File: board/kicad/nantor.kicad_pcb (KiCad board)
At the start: 2 copper layers, 139.5 x 94.4 mm, 26 parts, among them J1 Bridge, J2 Batt, SW1 Power, SW2 Power, U1 YAAJ_WeAct_BlackPill_Part_Like

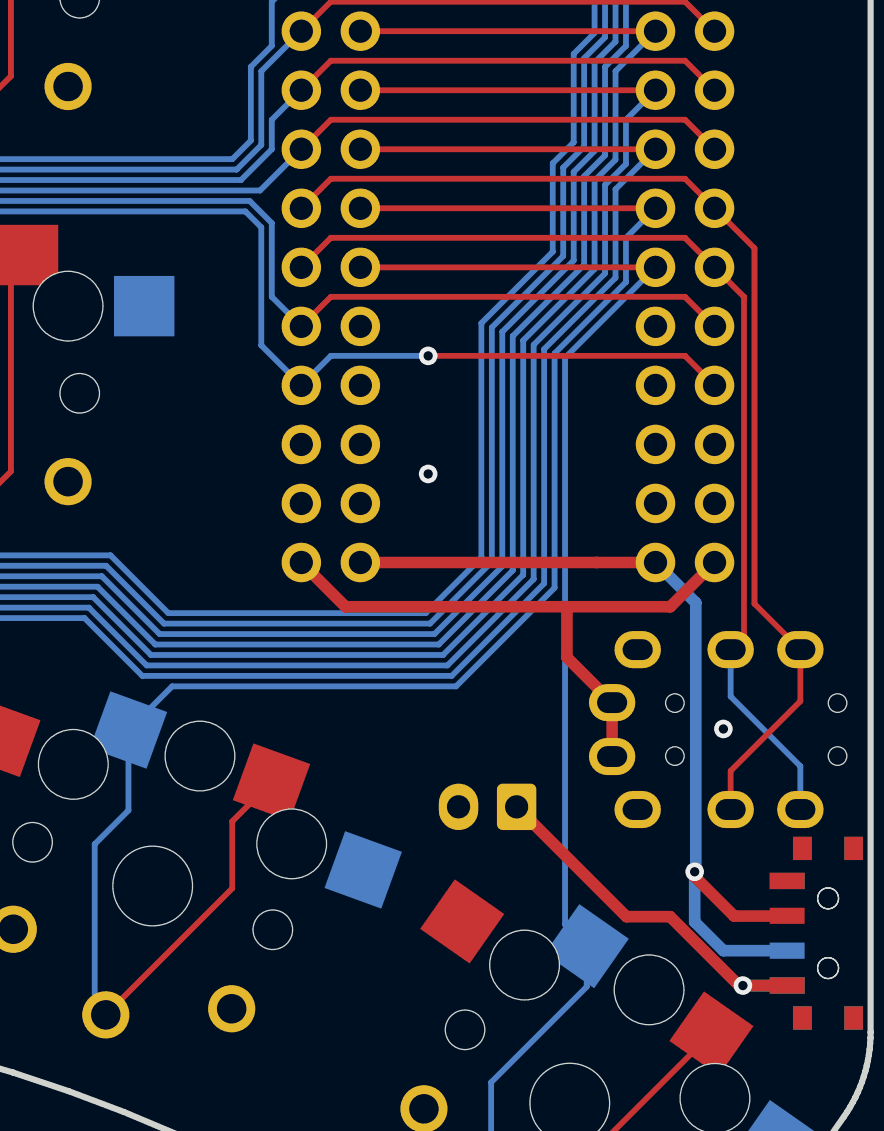
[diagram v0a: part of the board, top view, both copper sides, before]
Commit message: Move battery connector
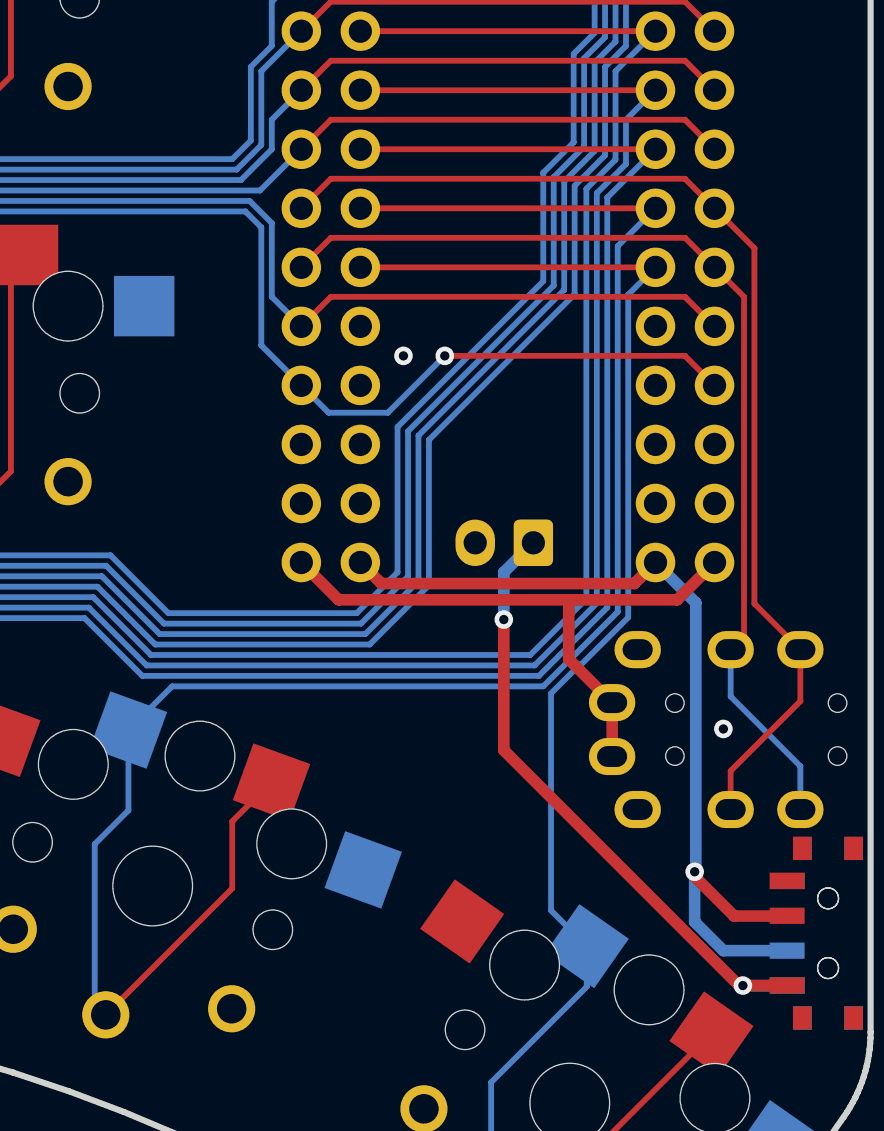
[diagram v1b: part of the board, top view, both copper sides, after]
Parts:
- moved J2 11.4 mm to (193.5, 104.7)
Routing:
- net Net-(J2-Pin_1): track 16.7 -> 27.7 mm, vias 1 -> 2
- net /k35: track 77.7 -> 79.9 mm
- net /k34: track 102.7 -> 104.9 mm
- net /k33: track 127.1 -> 129.3 mm
- net /k21: track 167.5 -> 169.7 mm
- net /k25: track 100.0 -> 98.3 mm
- net /k23: track 135.6 -> 133.8 mm
- net /k24: track 117.3 -> 115.6 mm
- net /k22: track 149.7 -> 148.0 mm
- net /k10: track 169.6 -> 170.5 mm
- net Net-(SW1-B): track 38.3 -> 39.0 mm
- net /k36: track 69.9 -> 70.5 mm

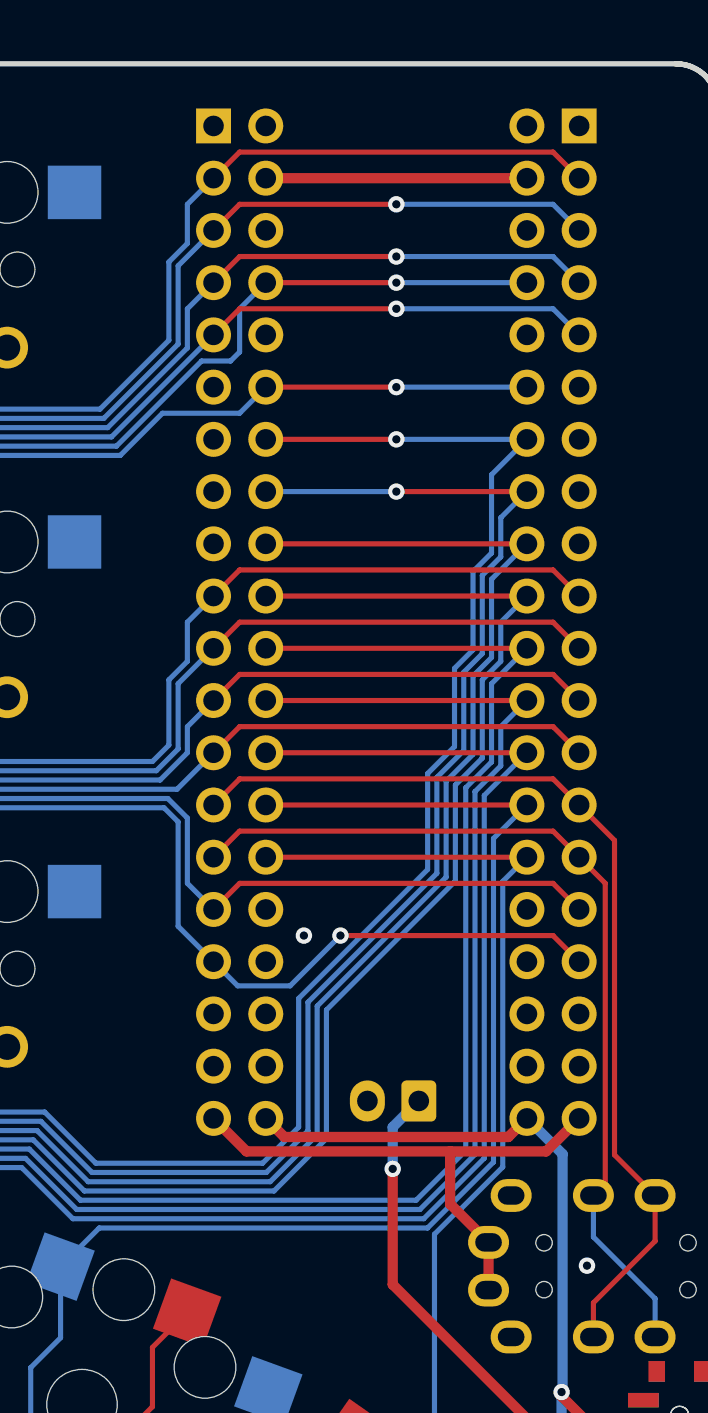
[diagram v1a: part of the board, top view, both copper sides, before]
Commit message: Add LEDs
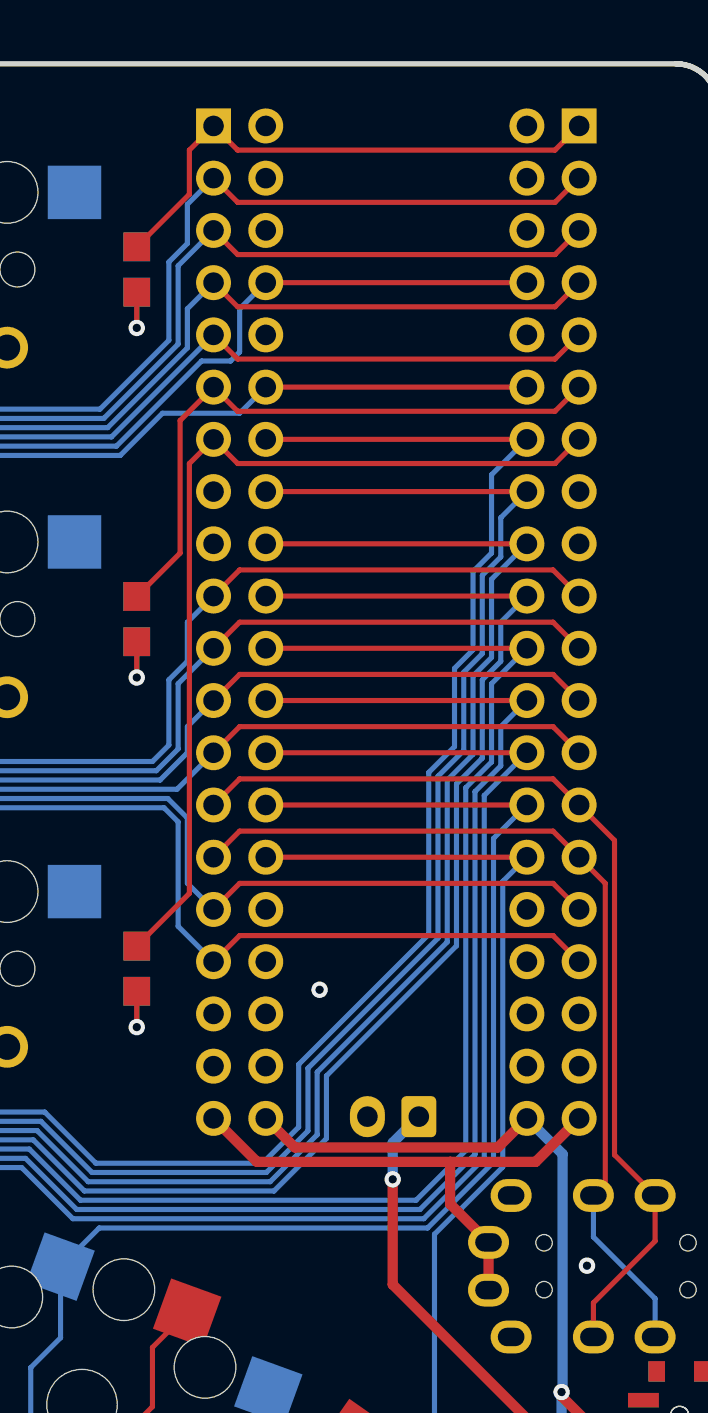
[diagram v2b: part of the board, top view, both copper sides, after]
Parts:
- added D1: LED, nantor:LED_0805, F.Cu at (179.8, 98.3)
- added D2: LED, nantor:LED_0805, F.Cu at (179.8, 81.3)
- added D3: LED, nantor:LED_0805, F.Cu at (179.8, 64.3)
- added R1: R, nantor:LED_0805, B.Cu at (179.8, 98.3)
- added R2: R, nantor:LED_0805, B.Cu at (179.8, 81.3)
- added R3: R, nantor:LED_0805, B.Cu at (179.8, 64.3)
- moved J2 0.76 mm to (193.5, 105.5)
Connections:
- net Net-(J2-Pin_1) renamed /BatPwr
- net Net-(SW1-B) renamed /BatActive
- net Net-(U1-PB6) renamed /TX
- net Net-(U1-PB7) renamed /RX
- U1 pad 1: unconnected-(U1-PB12-Pad1) -> /L3
- U1 pad 6: unconnected-(U1-PA9-Pad6) -> /L2
- U1 pad 7: unconnected-(U1-PA10-Pad7) -> /L1
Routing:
- net /L1: track 0.00 -> 44.9 mm
- net /L2: track 0.00 -> 30.5 mm
- net /L3: track 0.00 -> 26.2 mm
- net GND: track 12.7 -> 0.00 mm
- net Net-(D3-K): track 0.00 -> 3.48 mm, vias 0 -> 1
- net Net-(D2-K): track 0.00 -> 3.48 mm, vias 0 -> 1
- net Net-(D1-K): track 0.00 -> 3.48 mm, vias 0 -> 1
- net /k10: track 170.5 -> 169.6 mm, vias 1 -> 0
- net /BatPwr: track 27.7 -> 27.0 mm
- net /k25: track 98.3 -> 98.5 mm, vias 1 -> 0
- net /k04: vias 1 -> 0
- net /k03: vias 1 -> 0
- net /k02: vias 1 -> 0
- net /k24: vias 1 -> 0
- net /k01: vias 1 -> 0
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
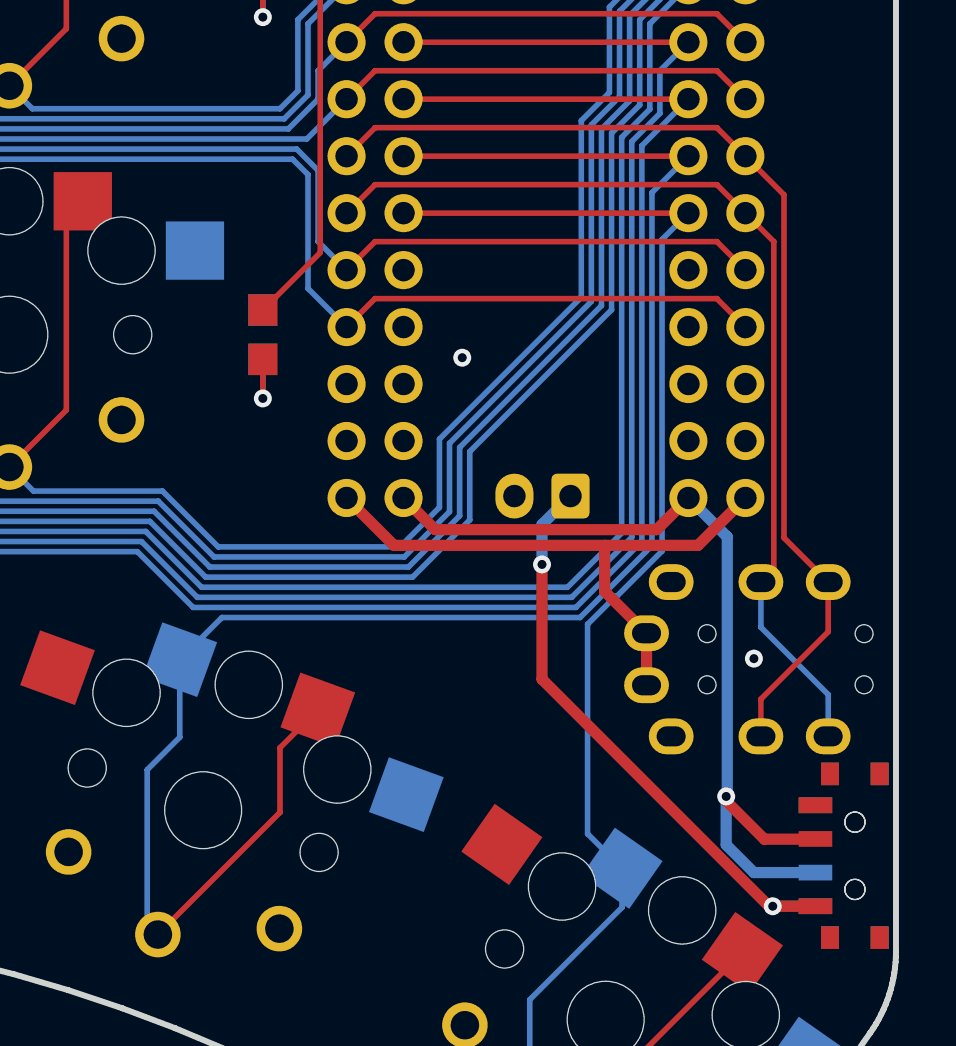
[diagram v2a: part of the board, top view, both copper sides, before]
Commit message: Reduce amount of vias
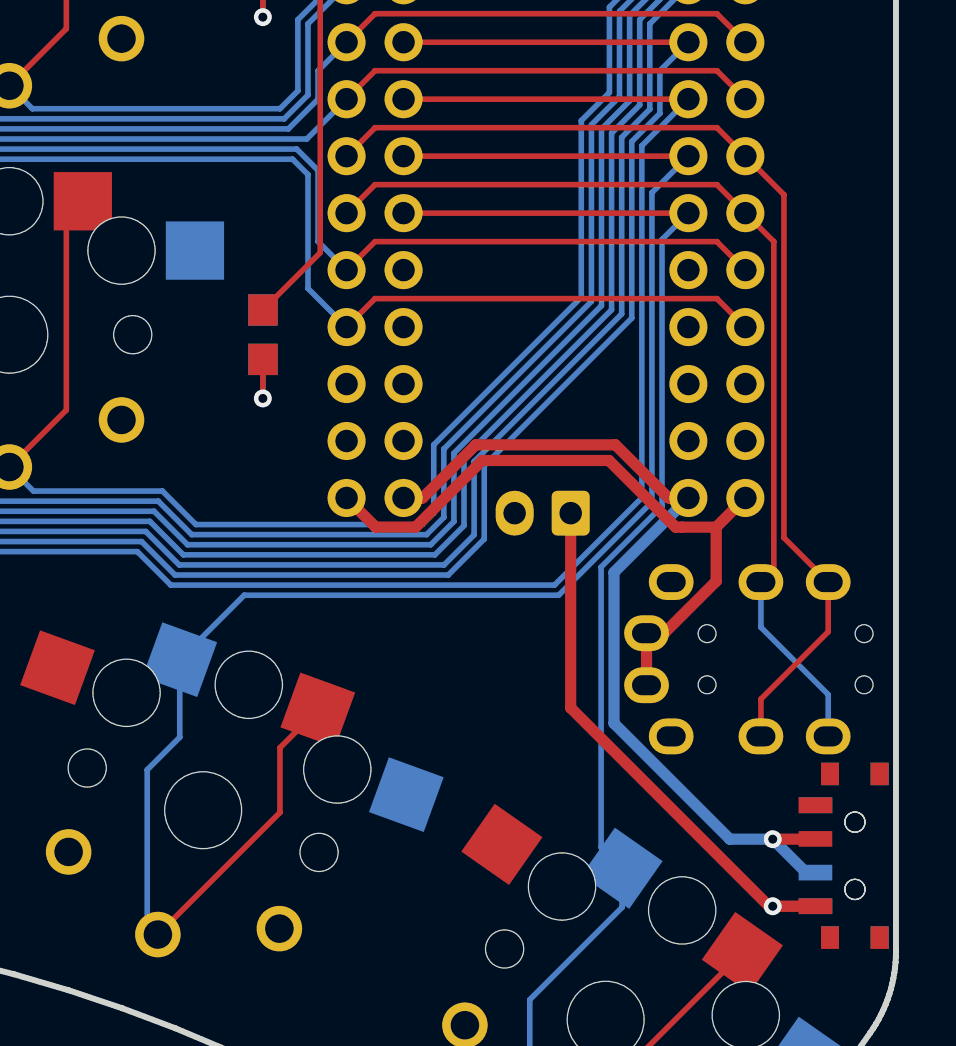
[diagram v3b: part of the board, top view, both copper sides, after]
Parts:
- moved J2 0.76 mm to (193.5, 106.2)
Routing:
- net /k33: track 129.3 -> 124.7 mm
- net /k21: track 169.7 -> 165.1 mm
- net +3.3V: track 26.5 -> 30.1 mm
- net /k34: track 104.9 -> 103.0 mm
- net /BatPwr: track 27.0 -> 25.2 mm, vias 2 -> 1
- net /k35: track 79.9 -> 78.8 mm
- net /k25: track 98.5 -> 97.7 mm
- net /k24: track 115.6 -> 114.7 mm
- net /k23: track 133.8 -> 133.0 mm
- net /k22: track 148.0 -> 147.2 mm
- net /k36: track 70.5 -> 69.9 mm
- net GND: vias 2 -> 0

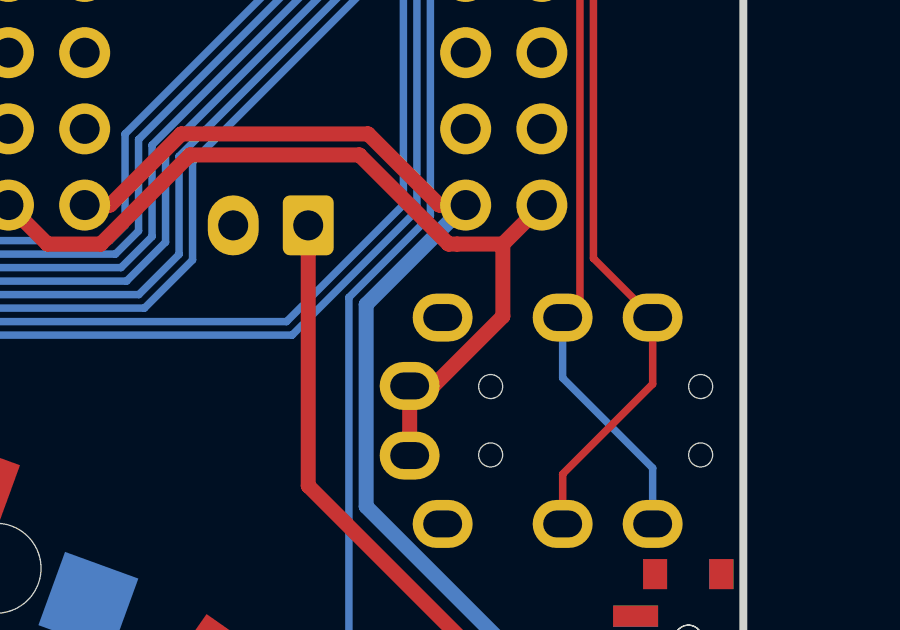
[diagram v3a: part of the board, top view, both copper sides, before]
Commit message: Increase ground plane
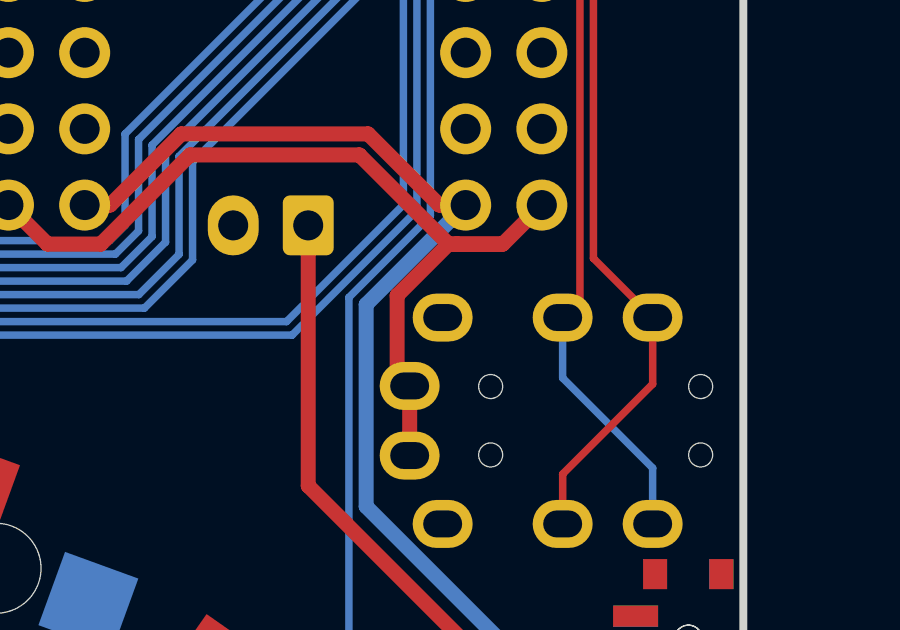
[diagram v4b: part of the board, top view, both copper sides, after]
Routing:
- net +3.3V: track 30.1 -> 31.1 mm
